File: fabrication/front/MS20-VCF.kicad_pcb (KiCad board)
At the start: 2 copper layers, 60 x 128.5 mm, 4 parts

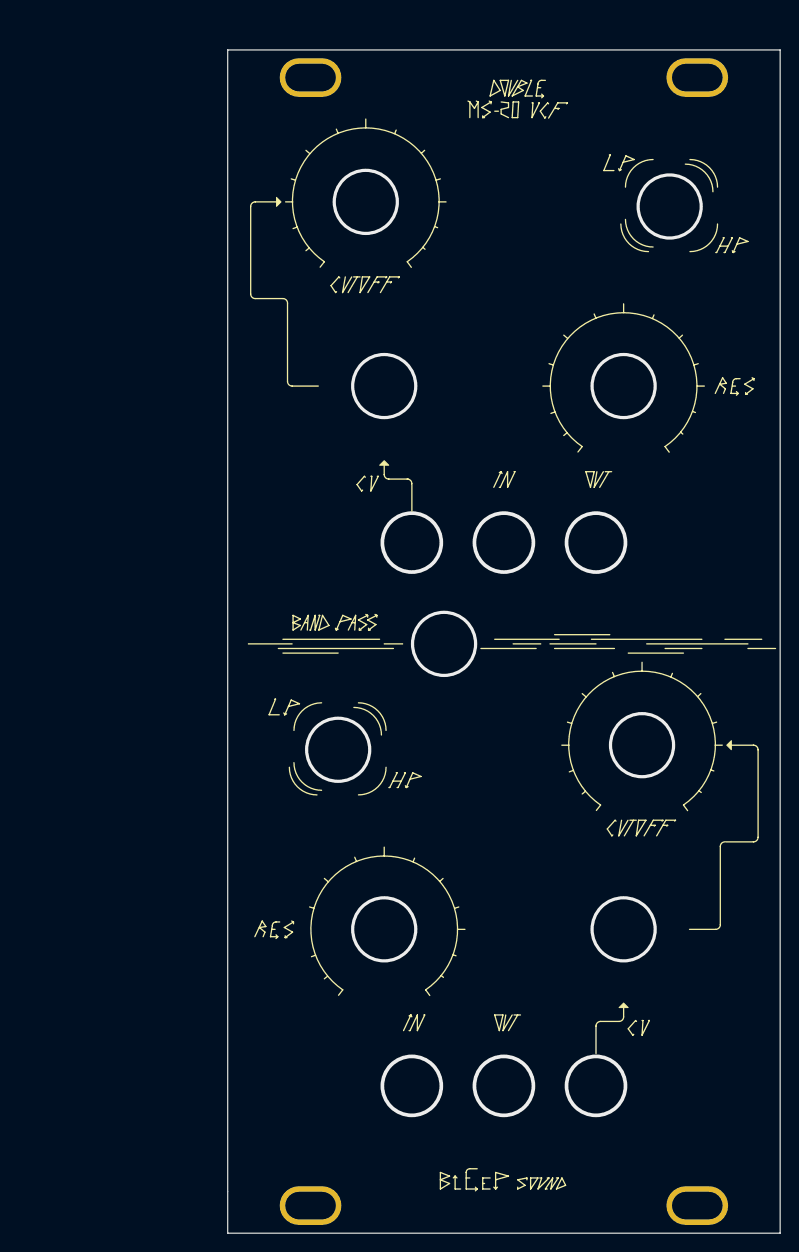
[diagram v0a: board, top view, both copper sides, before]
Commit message: update front panel and infos on components
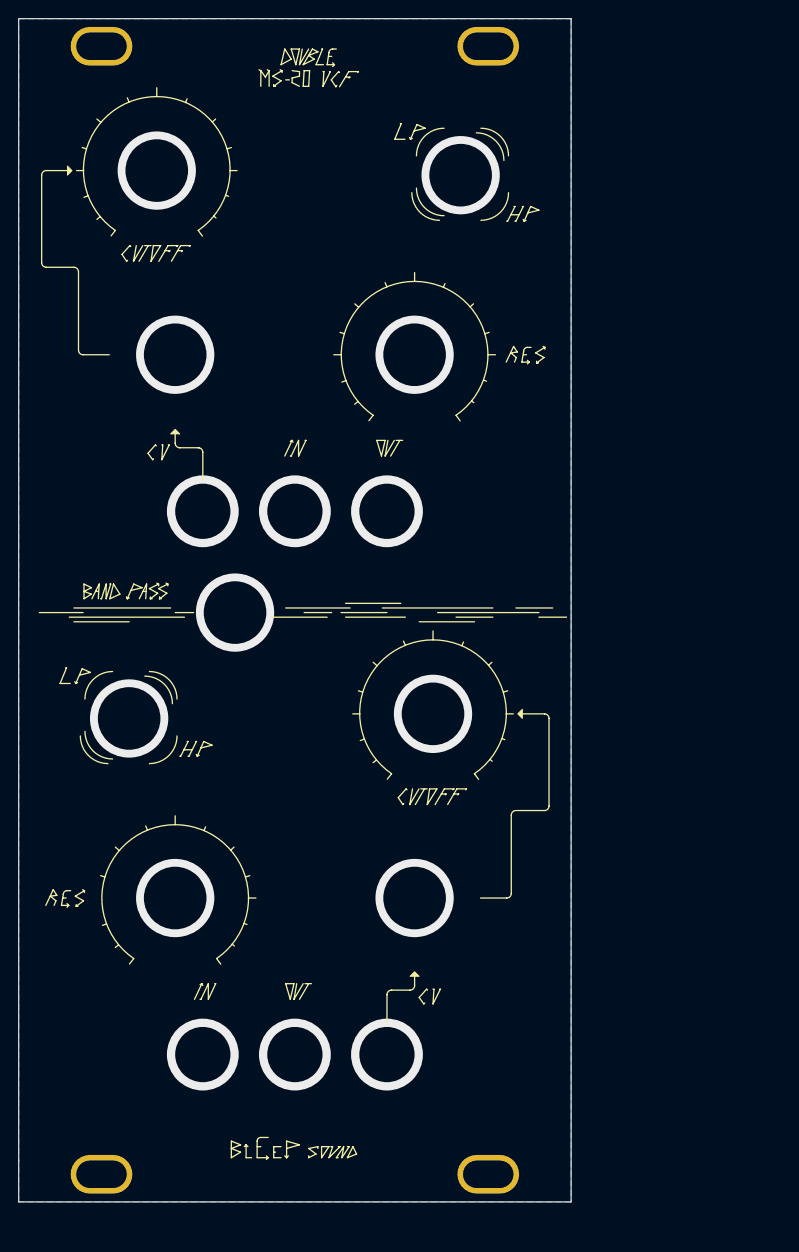
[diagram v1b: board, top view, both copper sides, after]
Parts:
- moved H1 23.0 mm to (56.2, 36.7)
- moved H2 23.0 mm to (98.2, 36.7)
- moved H3 23.0 mm to (98.2, 159.2)
- moved H4 23.0 mm to (56.2, 159.2)
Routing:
- added copper zone on B.Cu, net GND
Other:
- board text added: "Double MS-20 VCF V1.3 BleepSound 2023"
- board text removed: "Double MS-20 VCF V1.2 BleepSound 2022"

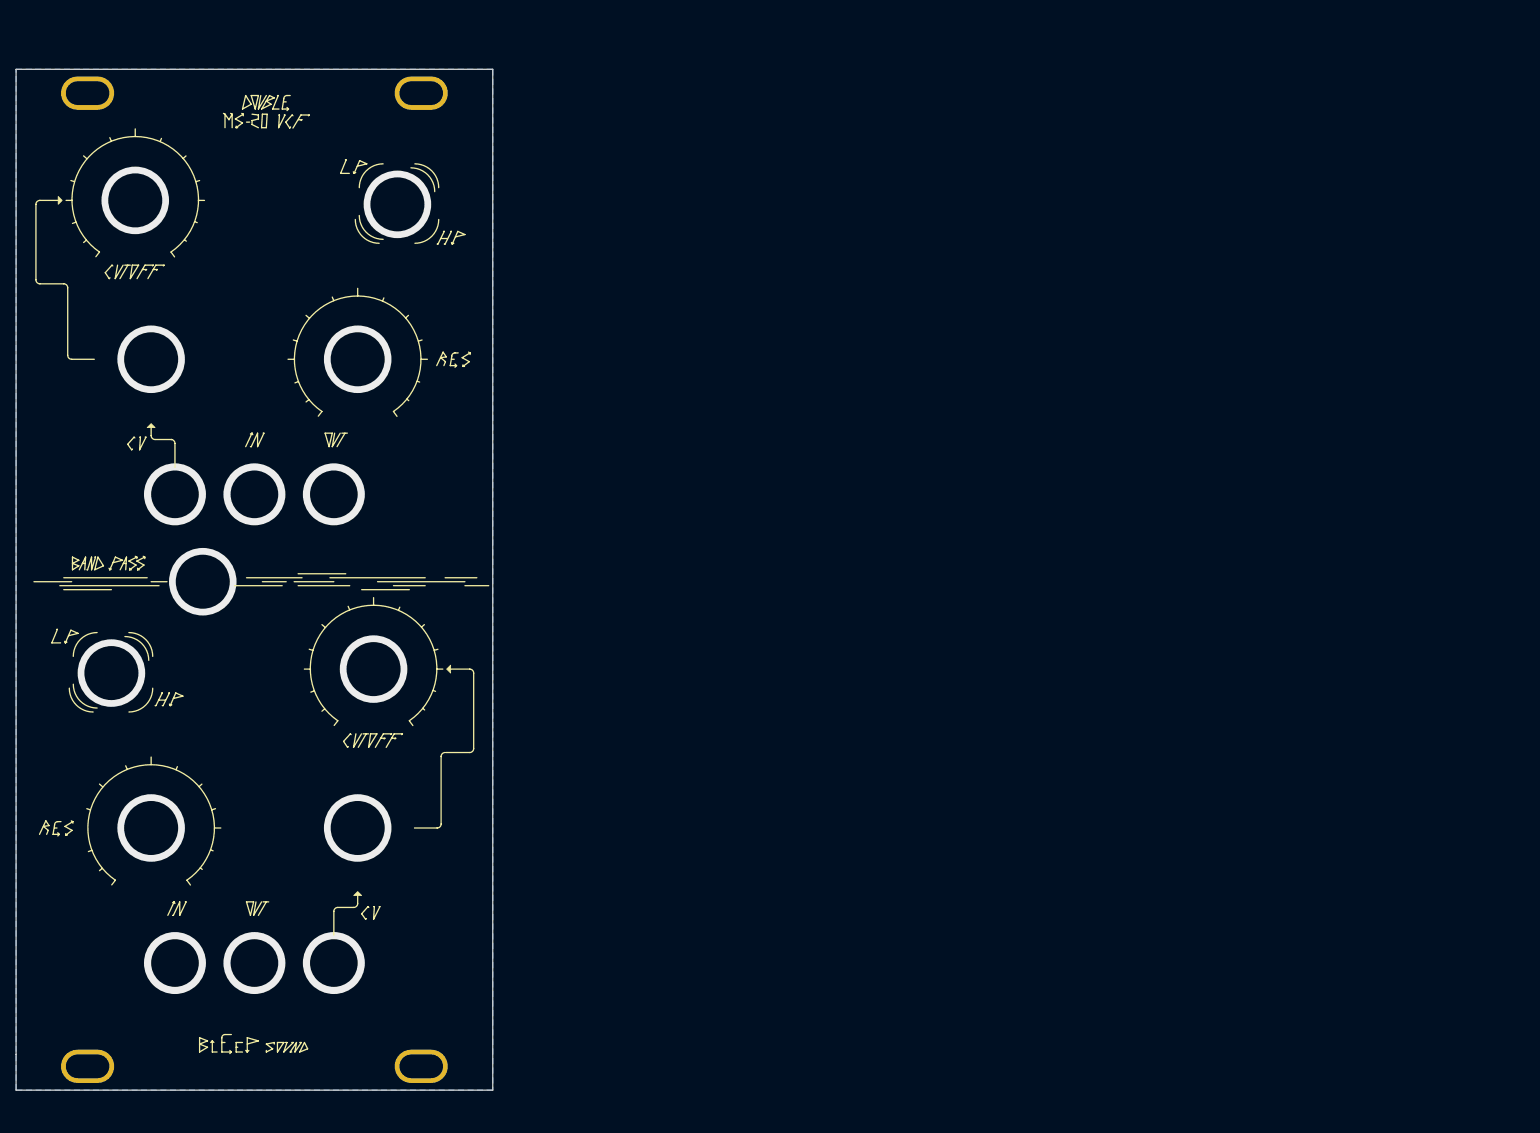
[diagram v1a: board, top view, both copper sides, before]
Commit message: update documentation + update repo layout
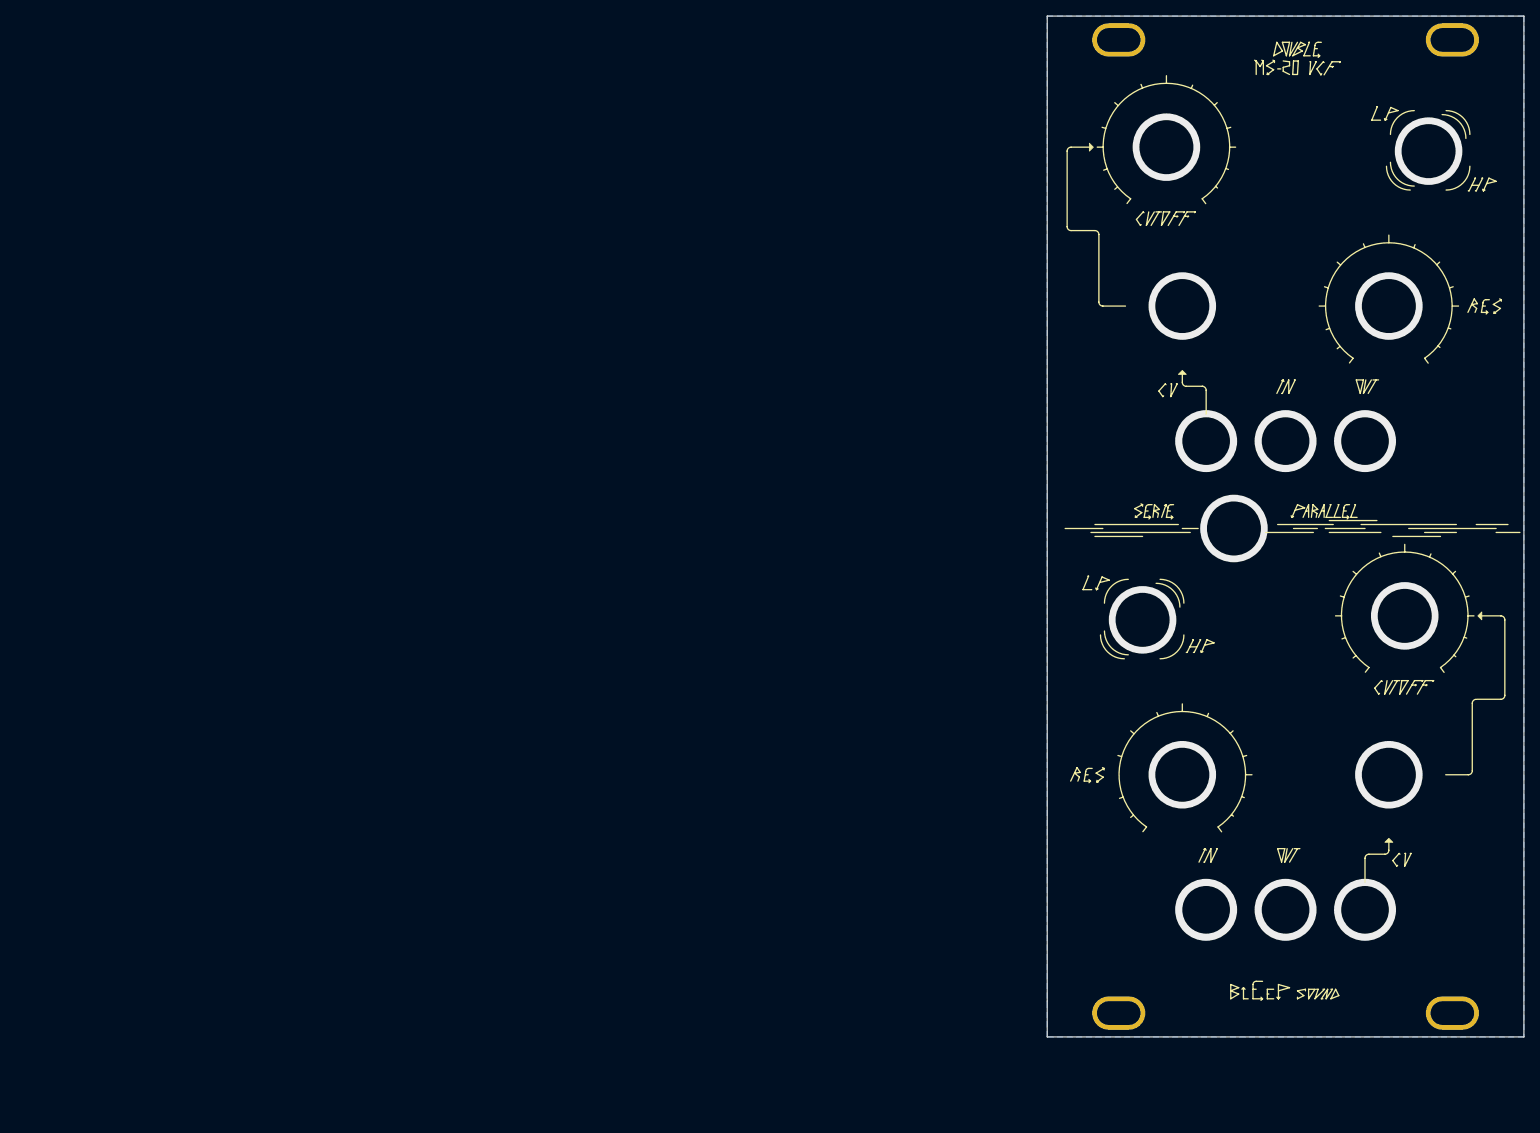
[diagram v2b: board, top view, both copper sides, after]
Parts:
- moved H1 130.0 mm to (186.0, 30.0)
- moved H2 130.0 mm to (228.0, 30.0)
- moved H3 130.0 mm to (228.0, 152.5)
- moved H4 130.0 mm to (186.0, 152.5)

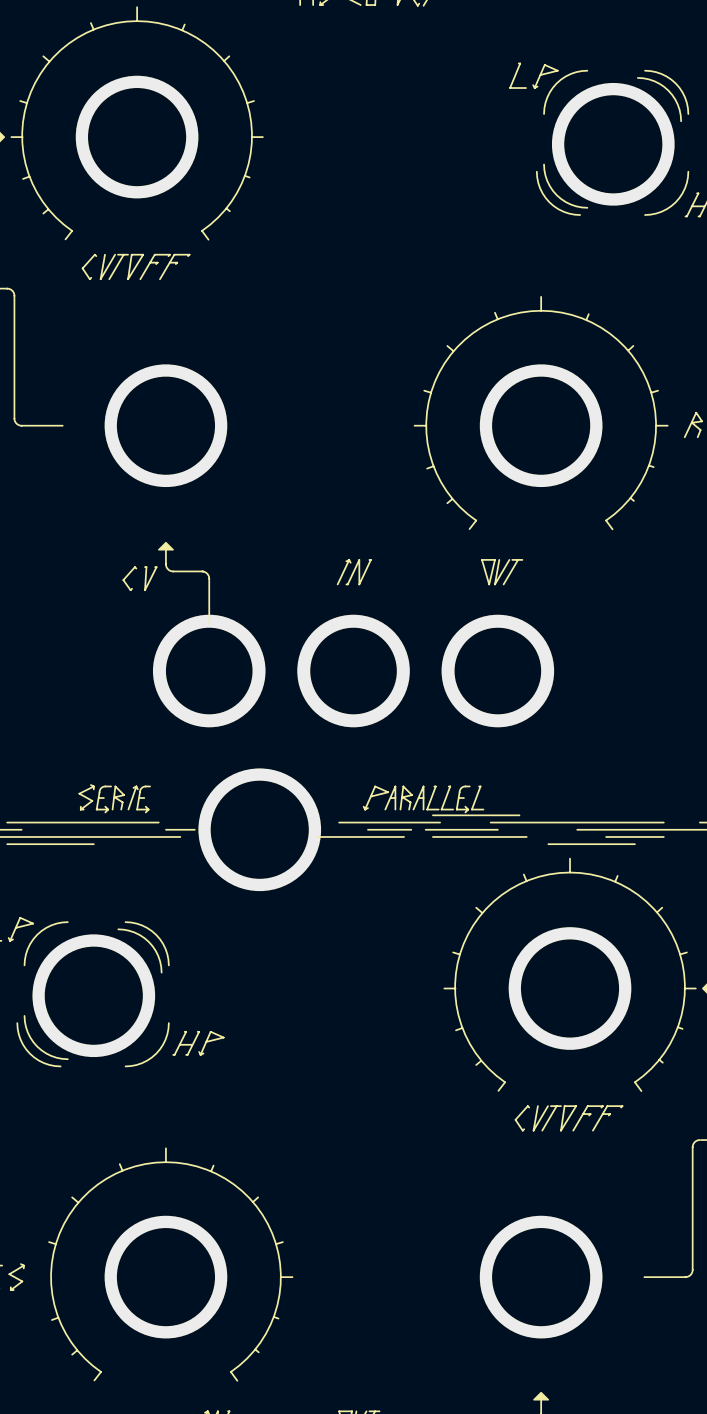
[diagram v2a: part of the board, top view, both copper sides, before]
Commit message: update version number + hole size on front panel
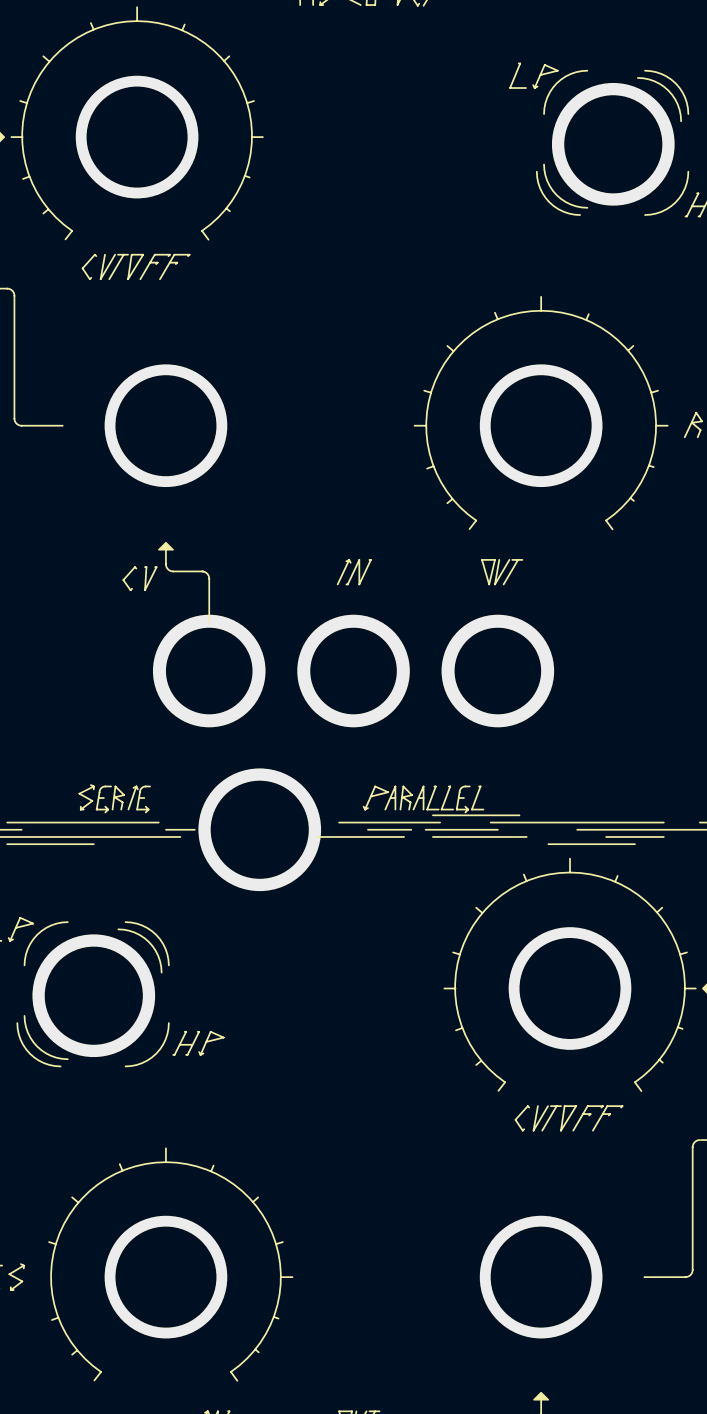
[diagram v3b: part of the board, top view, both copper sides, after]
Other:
- board text added: "Double MS-20 VCF V1.4 BleepSound 2023"
- board text removed: "Double MS-20 VCF V1.3 BleepSound 2023"
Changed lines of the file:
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@@
   (gr_line (start 177 27) (end 237 27)
     (stroke (width 0.05) (type solid)) (layer "Edge.Cuts"))
-  (gr_text "Double MS-20 VCF\nV1.3 BleepSound\n2023" (at 208 32.65) (layer "B.SilkS")
+  (gr_text "Double MS-20 VCF\nV1.4 BleepSound\n2023" (at 208 32.65) (layer "B.SilkS")
     (effects (font (size 1 1) (thickness 0.15)) (justify mirror))
   )
@@
   (via (at 225 44) (size 8.5) (drill 6.8) (layers "F.Cu" "B.Cu") (net 1))
   (via (at 189 103) (size 8.5) (drill 6.8) (layers "F.Cu" "B.Cu") (net 1))
-  (via (at 220 122.5) (size 8.5) (drill 6.8) (layers "F.Cu" "B.Cu") (net 1))
-  (via (at 194 122.5) (size 8.5) (drill 6.8) (layers "F.Cu" "B.Cu") (net 1))
-  (via (at 222 102.5) (size 8.5) (drill 6.8) (layers "F.Cu" "B.Cu") (net 1))
+  (via (at 220 122.5) (size 8.5) (drill 7) (layers "F.Cu" "B.Cu") (net 1))
+  (via (at 194 122.5) (size 8.5) (drill 7) (layers "F.Cu" "B.Cu") (net 1))
+  (via (at 222 102.5) (size 8.5) (drill 7) (layers "F.Cu" "B.Cu") (net 1))
   (via (at 207 139.5) (size 7.8) (drill 6) (layers "F.Cu" "B.Cu") (net 1))
   (via (at 197 139.5) (size 7.8) (drill 6) (layers "F.Cu" "B.Cu") (net 1))
   (via (at 217 139.5) (size 7.8) (drill 6) (layers "F.Cu" "B.Cu") (net 1))
-  (via (at 220 63.5) (size 8.5) (drill 6.8) (layers "F.Cu" "B.Cu") (net 1))
-  (via (at 194 63.5) (size 8.5) (drill 6.8) (layers "F.Cu" "B.Cu") (net 1))
-  (via (at 192 43.5) (size 8.5) (drill 6.8) (layers "F.Cu" "B.Cu") (net 1))
+  (via (at 220 63.5) (size 8.5) (drill 7) (layers "F.Cu" "B.Cu") (net 1))
+  (via (at 194 63.5) (size 8.5) (drill 7) (layers "F.Cu" "B.Cu") (net 1))
+  (via (at 192 43.5) (size 8.5) (drill 7) (layers "F.Cu" "B.Cu") (net 1))
   (zone (net 0) (net_name "") (layers "F&B.Cu") (hatch edge 0.508)
     (connect_pads (clearance 0))

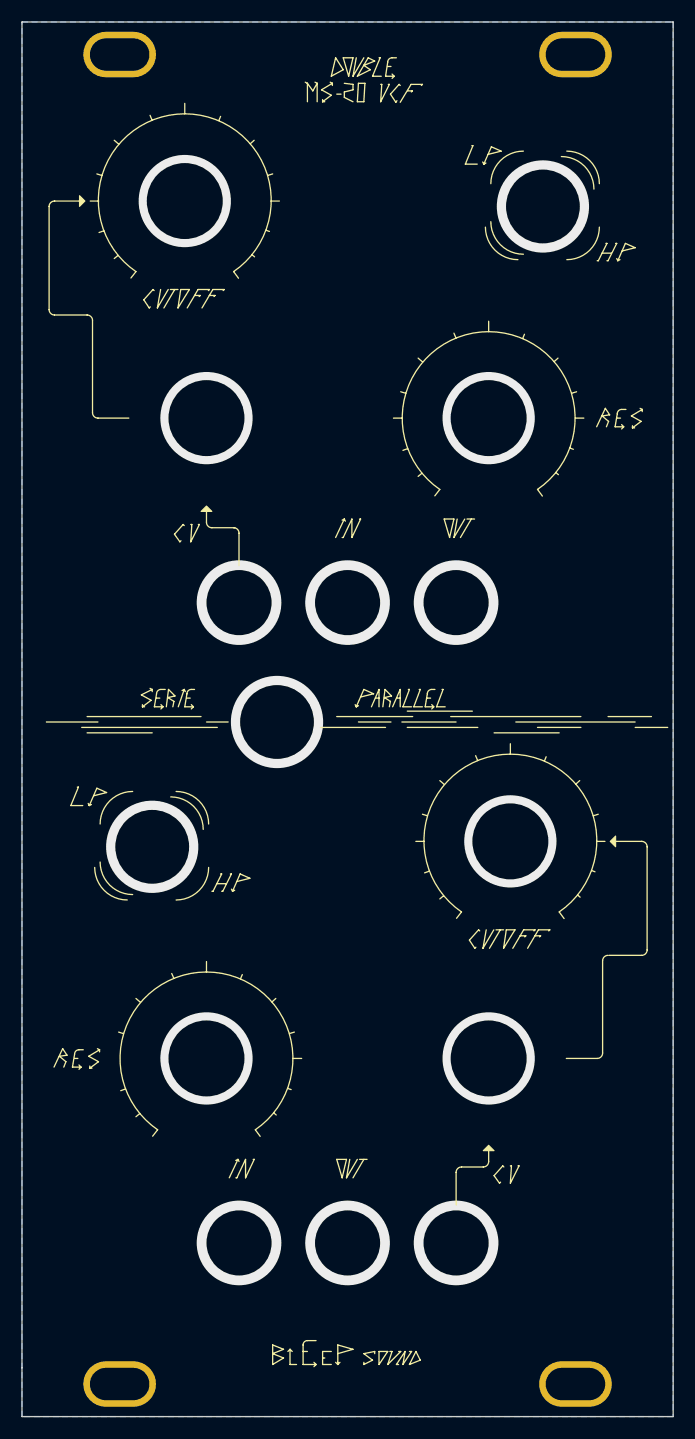
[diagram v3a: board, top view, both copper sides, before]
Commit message: V2.0
new front panel layout
new normalisation for CV and in/out for bandpass filter
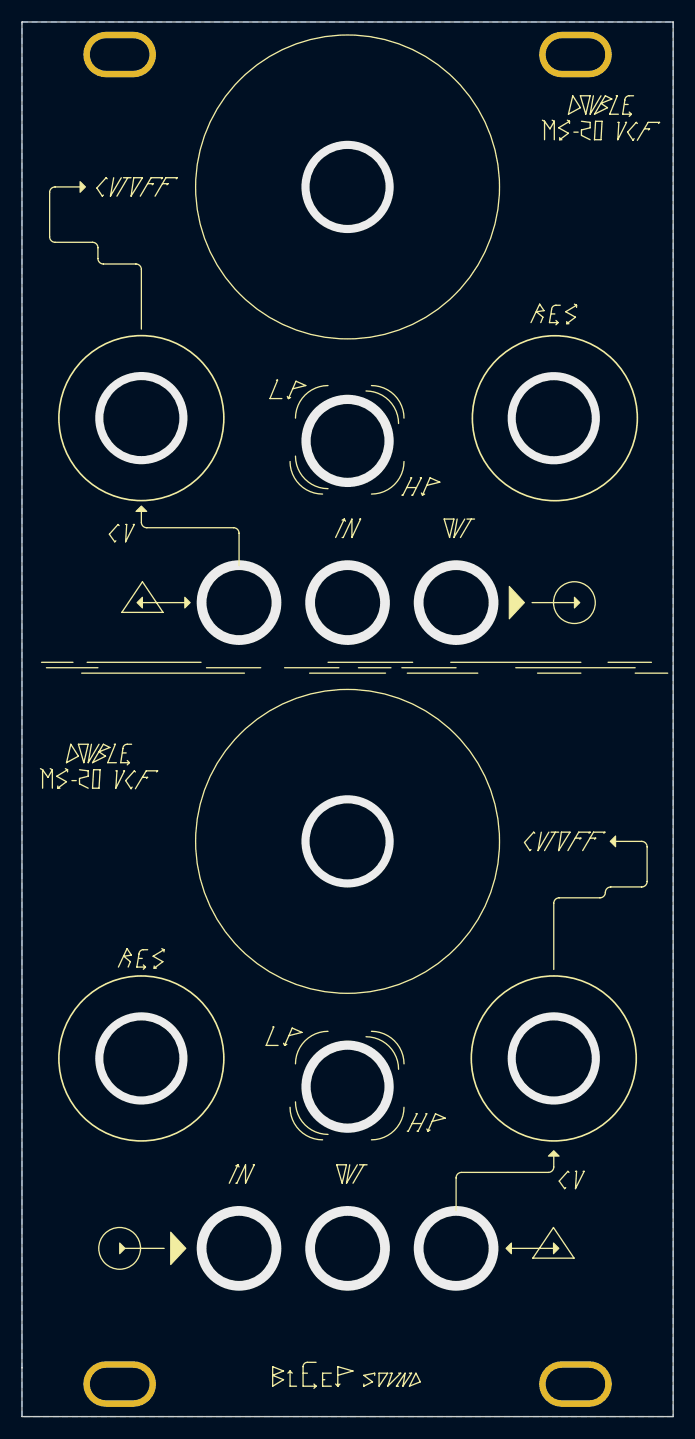
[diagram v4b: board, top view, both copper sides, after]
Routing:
- net GND: vias 15 -> 14
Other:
- board text added: "Double MS-20 VCF V2.0 BleepSound 2025"
- board text removed: "Double MS-20 VCF V1.4 BleepSound 2023"
